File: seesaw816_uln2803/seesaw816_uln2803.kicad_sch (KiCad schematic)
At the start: 36 parts, among them J1 Screw_Terminal_01x02, J10 Conn_01x10_Female, J11 Conn_01x10_Female, J12 DIP Socket, J13 Conn_01x02_Male, J14 Conn_01x02_Male, J15 40pin break-away, J2 Screw_Terminal_01x02, J3 Screw_Terminal_01x02, J4 Screw_Terminal_01x02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

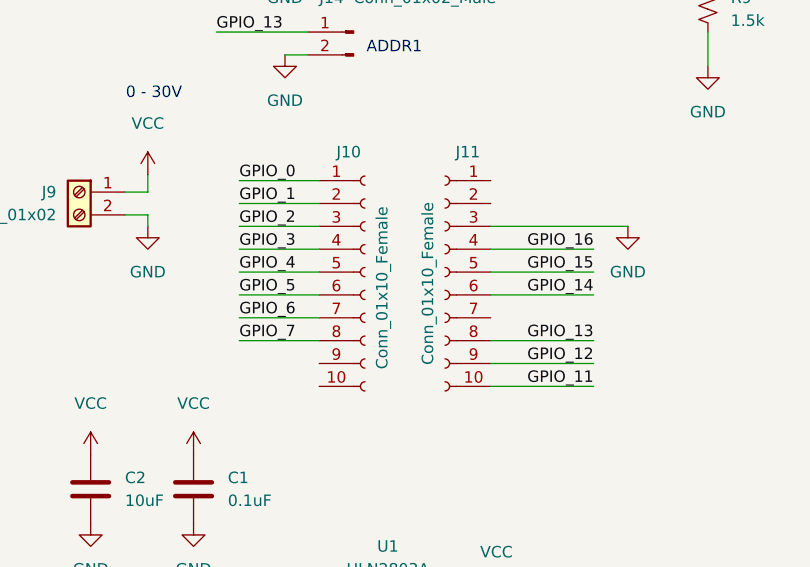
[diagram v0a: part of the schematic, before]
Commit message: update to Kicad 7, update BOM
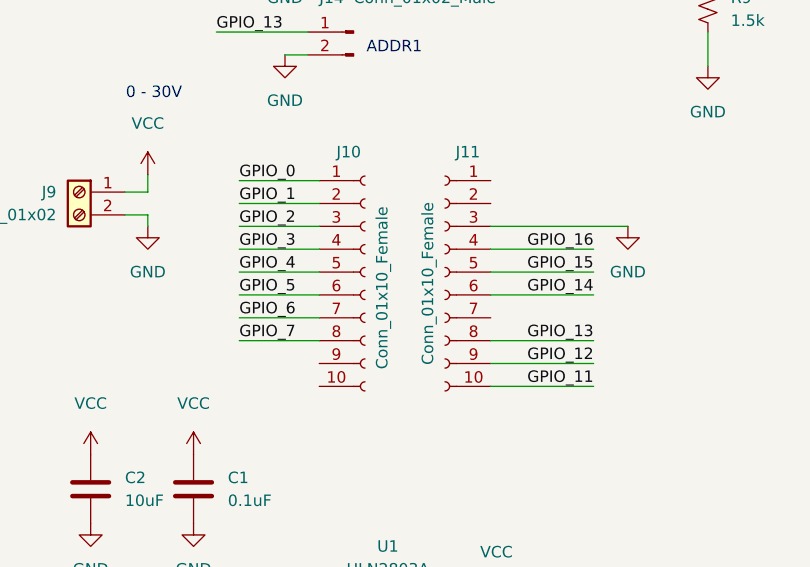
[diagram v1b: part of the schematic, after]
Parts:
- J1, J2, J3, J4, J5, J6, J7, J8, J9: Mfg (none) -> TE; Part (none) -> 282834-2
- J10, J11: Mfg (none) -> Sullins; Part (none) -> PPPC101LFBN-RC
- R1, R2, R3, R4, R5, R6, R7, R8, R9: Mfg (none) -> Yageo; Part (none) -> RC0805FR-071K5L
- U1: Mfg (none) -> ST; Part (none) -> ULN2803A
